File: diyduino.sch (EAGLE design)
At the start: 22 parts, among them Q2 16MHz

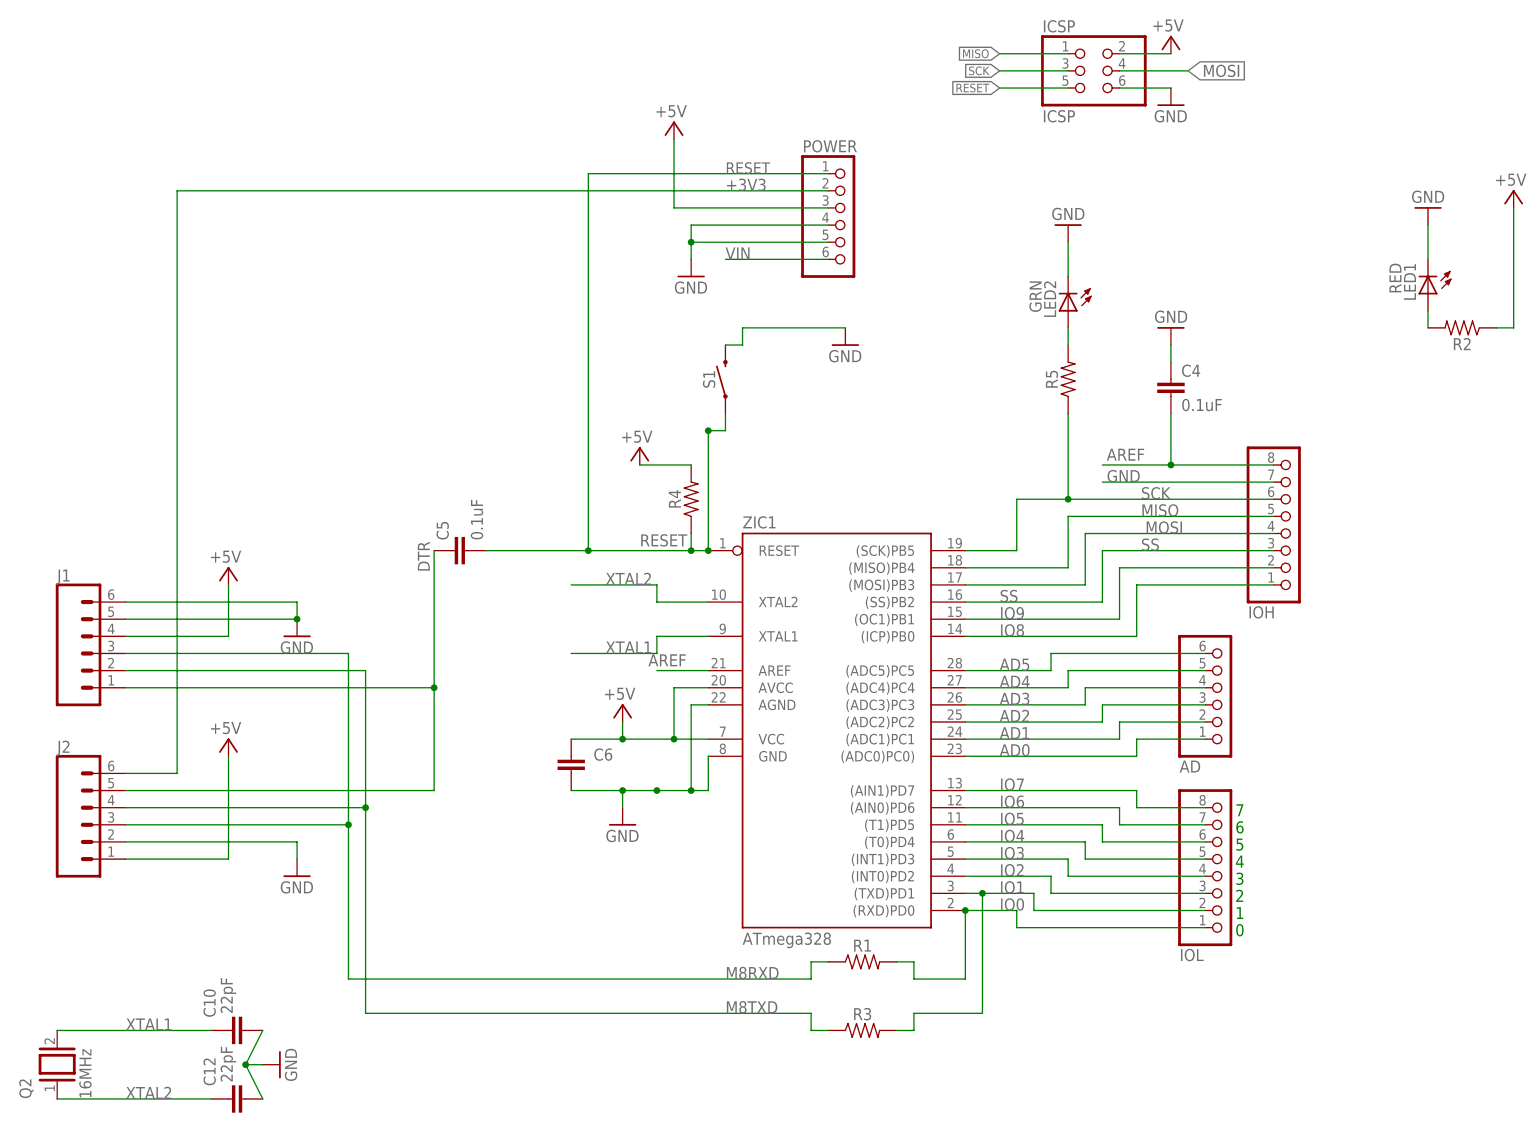
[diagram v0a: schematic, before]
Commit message: 0.3.0 changes, fixed CH340 pinout, changed crystal to resonator
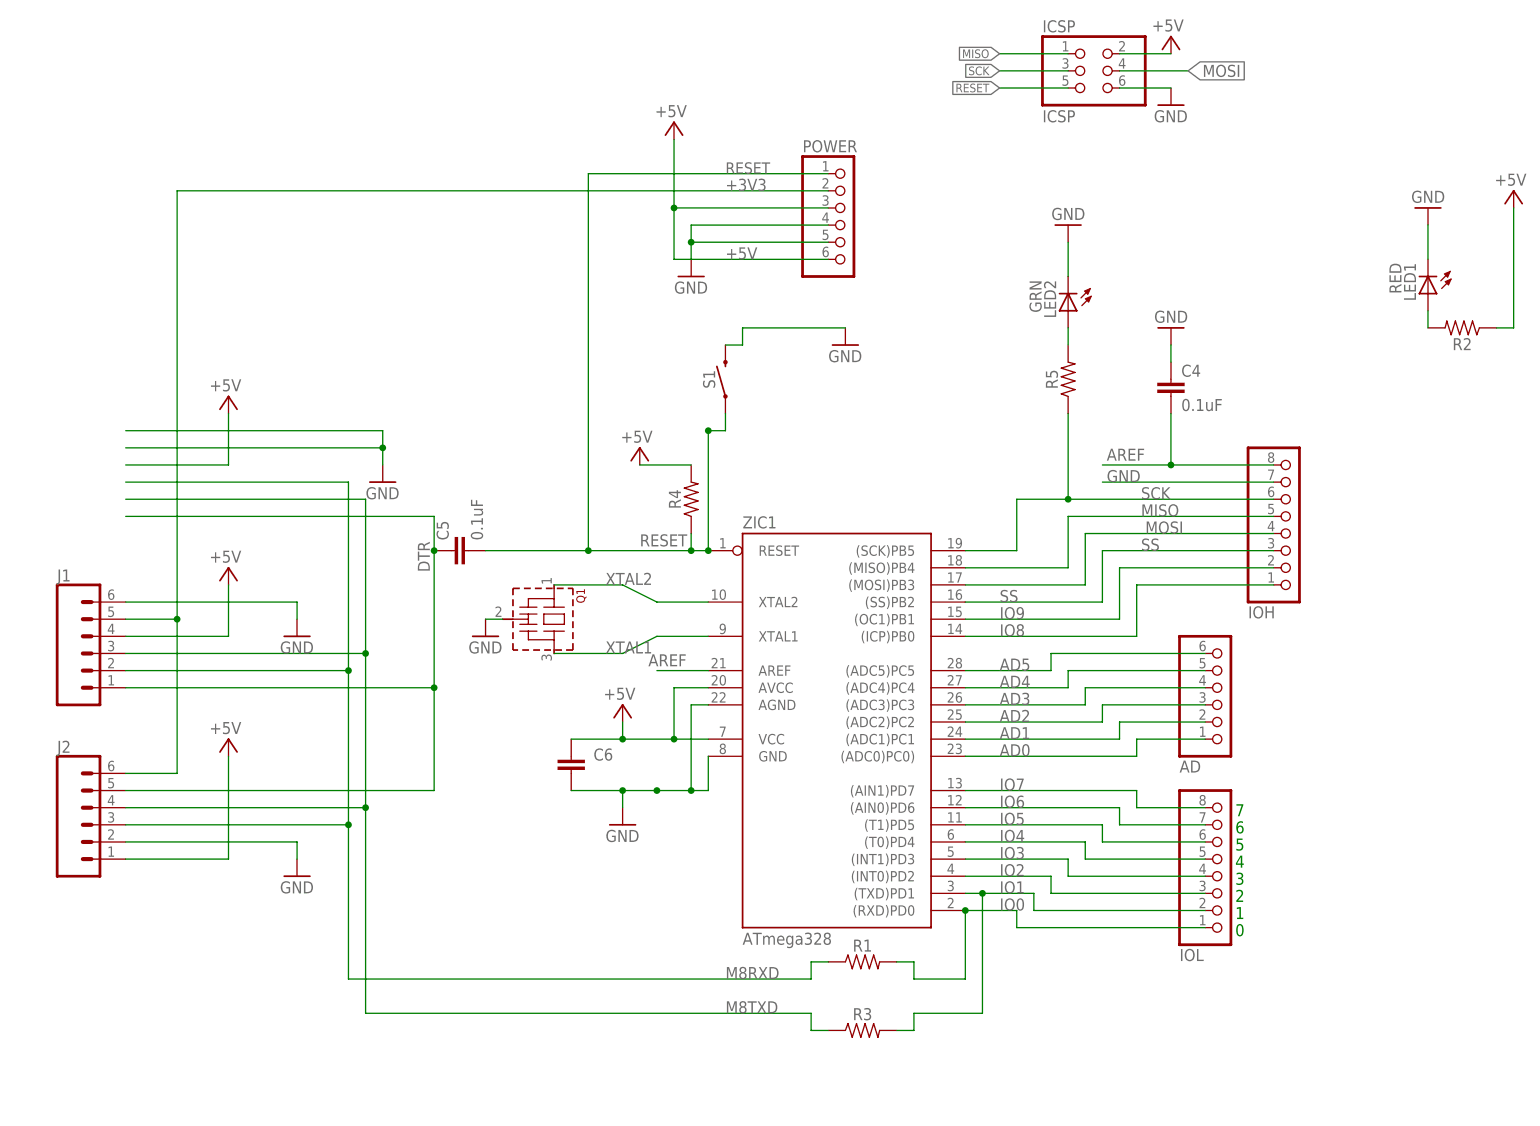
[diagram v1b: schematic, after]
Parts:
- removed C10, C12: 22pF, SparkFun-Capacitors:22PF-PTH-2.54MM-200V-5%
- removed Q2: 16MHz, special:XTAL/S
- added Q1: (no value), murata-resonators:CSTLS_X
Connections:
- removed net VIN: POWER.6
- net +3V3: now also J1.5
- net +5V: now also POWER.6
- net GND: now also Q1.VSS; no longer C10.1, C12.1, J1.5
- net M8RXD: now also J1.2; no longer J1.3
- net M8TXD: now also J1.3; no longer J1.2
- net XTAL1: now also Q1.3; no longer C10.2, Q2.2
- net XTAL2: now also Q1.1; no longer C12.2, Q2.1

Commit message: adding dinosaur!
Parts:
- renumbered C4 to C3, C5 to C1, C6 to C2
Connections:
- net +5V: now also R3.1, R5.2; no longer R2.1, R4.2
- net IO1: now also R2.2; no longer R3.2
- net M8TXD: now also R2.1; no longer R3.1
- net N$1: now also R4.2; no longer R5.2
- net N$2: now also R3.2; no longer R2.2
- net RESET: now also R5.1; no longer R4.1
- net SCK: now also R4.1; no longer R5.1
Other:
- moved on the sheet: R2, R3, R4, R5
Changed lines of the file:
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@@
 <part name="GND12" library="supply1" library_urn="urn:adsk.eagle:library:371" deviceset="GND" device=""/>
 <part name="POWER" library="pinhead" library_urn="urn:adsk.eagle:library:325" deviceset="PINHD-1X6" device="" package3d_urn="urn:adsk.eagle:package:22472/2"/>
-<part name="C4" library="capacitor-wima" library_urn="urn:adsk.eagle:library:116" deviceset="C" device="2.5/2" package3d_urn="urn:adsk.eagle:package:5415/1" value="0.1uF"/>
+<part name="C3" library="capacitor-wima" library_urn="urn:adsk.eagle:library:116" deviceset="C" device="2.5/2" package3d_urn="urn:adsk.eagle:package:5415/1" value="0.1uF"/>
 <part name="GND13" library="supply1" library_urn="urn:adsk.eagle:library:371" deviceset="GND" device=""/>
 <part name="LED2" library="adafruit" deviceset="LED" device="3MM" value="GRN"/>
 <part name="GND17" library="supply1" library_urn="urn:adsk.eagle:library:371" deviceset="GND" device=""/>
-<part name="C5" library="capacitor-wima" library_urn="urn:adsk.eagle:library:116" deviceset="C" device="2.5/2" package3d_urn="urn:adsk.eagle:package:5415/1" value="0.1uF"/>
-<part name="C6" library="capacitor-wima" library_urn="urn:adsk.eagle:library:116" deviceset="C" device="2.5/2" package3d_urn="urn:adsk.eagle:package:5415/1" value="0.1uF"/>
+<part name="C1" library="capacitor-wima" library_urn="urn:adsk.eagle:library:116" deviceset="C" device="2.5/2" package3d_urn="urn:adsk.eagle:package:5415/1" value="0.1uF"/>
+<part name="C2" library="capacitor-wima" library_urn="urn:adsk.eagle:library:116" deviceset="C" device="2.5/2" package3d_urn="urn:adsk.eagle:package:5415/1" value="0.1uF"/>
 <part name="R1" library="SparkFun-Resistors" library_urn="urn:adsk.eagle:library:532" deviceset="RESISTOR" device="AXIAL-0.3" package3d_urn="urn:adsk.eagle:package:39658/1" value=" "/>
-<part name="R3" library="SparkFun-Resistors" library_urn="urn:adsk.eagle:library:532" deviceset="RESISTOR" device="AXIAL-0.3" package3d_urn="urn:adsk.eagle:package:39658/1" value=" "/>
+<part name="R2" library="SparkFun-Resistors" library_urn="urn:adsk.eagle:library:532" deviceset="RESISTOR" device="AXIAL-0.3" package3d_urn="urn:adsk.eagle:package:39658/1" value=" "/>
+<part name="R5" library="SparkFun-Resistors" library_urn="urn:adsk.eagle:library:532" deviceset="RESISTOR" device="AXIAL-0.3" package3d_urn="urn:adsk.eagle:package:39658/1" value=" "/>
 <part name="R4" library="SparkFun-Resistors" library_urn="urn:adsk.eagle:library:532" deviceset="RESISTOR" device="AXIAL-0.3" package3d_urn="urn:adsk.eagle:package:39658/1" value=" "/>
-<part name="R5" library="SparkFun-Resistors" library_urn="urn:adsk.eagle:library:532" deviceset="RESISTOR" device="AXIAL-0.3" package3d_urn="urn:adsk.eagle:package:39658/1" value=" "/>
 <part name="J1" library="SparkFun-Connectors" library_urn="urn:adsk.eagle:library:513" deviceset="CONN_06" device="SILK_FEMALE_PTH" package3d_urn="urn:adsk.eagle:package:38009/1"/>
 <part name="GND4" library="supply1" library_urn="urn:adsk.eagle:library:371" deviceset="GND" device=""/>
@@
 <part name="LED1" library="adafruit" deviceset="LED" device="3MM" value="RED"/>
 <part name="GND6" library="supply1" library_urn="urn:adsk.eagle:library:371" deviceset="GND" device=""/>
-<part name="R2" library="SparkFun-Resistors" library_urn="urn:adsk.eagle:library:532" deviceset="RESISTOR" device="AXIAL-0.3" package3d_urn="urn:adsk.eagle:package:39658/1" value=" "/>
+<part name="R3" library="SparkFun-Resistors" library_urn="urn:adsk.eagle:library:532" deviceset="RESISTOR" device="AXIAL-0.3" package3d_urn="urn:adsk.eagle:package:39658/1" value=" "/>
 <part name="P+7" library="supply1" library_urn="urn:adsk.eagle:library:371" deviceset="+5V" device=""/>
 <part name="P+8" library="supply1" library_urn="urn:adsk.eagle:library:371" deviceset="+5V" device=""/>
@@
 <instance part="GND12" gate="1" x="157.48" y="109.22"/>
 <instance part="POWER" gate="A" x="157.48" y="127"/>
-<instance part="C4" gate="G$1" x="205.74" y="104.14"/>
+<instance part="C3" gate="G$1" x="205.74" y="104.14"/>
 <instance part="GND13" gate="1" x="205.74" y="111.76" rot="R180"/>
 <instance part="LED2" gate="G$1" x="190.5" y="114.3" rot="R180"/>
 <instance part="GND17" gate="1" x="190.5" y="127" rot="R180"/>
-<instance part="C5" gate="G$1" x="99.06" y="78.74" rot="R90"/>
-<instance part="C6" gate="G$1" x="116.84" y="45.72" smashed="yes" rot="MR180">
+<instance part="C1" gate="G$1" x="99.06" y="78.74" rot="R90"/>
+<instance part="C2" gate="G$1" x="116.84" y="45.72" smashed="yes" rot="MR180">
 <attribute name="NAME" x="123.063" y="47.625" size="1.778" layer="95" rot="MR0"/>
 </instance>
 <instance part="R1" gate="G$1" x="160.02" y="17.78"/>
-<instance part="R3" gate="G$1" x="160.02" y="7.62"/>
-<instance part="R4" gate="G$1" x="134.62" y="86.36" rot="R90"/>
-<instance part="R5" gate="G$1" x="190.5" y="104.14" rot="R90"/>
+<instance part="R2" gate="G$1" x="160.02" y="7.62"/>
+<instance part="R5" gate="G$1" x="134.62" y="86.36" rot="R90"/>
+<instance part="R4" gate="G$1" x="190.5" y="104.14" rot="R90"/>
 <instance part="J1" gate="G$1" x="45.72" y="63.5"/>
 <instance part="GND4" gate="1" x="76.2" y="66.04"/>
@@
 <instance part="LED1" gate="G$1" x="243.84" y="116.84" rot="R180"/>
 <instance part="GND6" gate="1" x="243.84" y="129.54" rot="R180"/>
-<instance part="R2" gate="G$1" x="248.92" y="111.76" rot="R180"/>
+<instance part="R3" gate="G$1" x="248.92" y="111.76" rot="R180"/>
 <instance part="P+7" gate="1" x="256.54" y="132.08" smashed="yes">
 <attribute name="VALUE" x="258.445" y="134.62" size="1.778" layer="96" rot="R180"/>
@@
 <wire x1="127" y1="91.44" x2="134.62" y2="91.44" width="0.1524" layer="91"/>
 <pinref part="P+2" gate="1" pin="+5V"/>
-<pinref part="R4" gate="G$1" pin="2"/>
+<pinref part="R5" gate="G$1" pin="2"/>
 </segment>
 <segment>
@@
 <pinref part="P+3" gate="1" pin="+5V"/>
 <pinref part="ZIC1" gate="G$1" pin="AVCC"/>
-<pinref part="C6" gate="G$1" pin="2"/>
+<pinref part="C2" gate="G$1" pin="2"/>
 </segment>
 <segment>
@@
 </segment>
 <segment>
-<pinref part="R2" gate="G$1" pin="1"/>
+<pinref part="R3" gate="G$1" pin="1"/>
 <pinref part="P+7" gate="1" pin="+5V"/>
 <wire x1="254" y1="111.76" x2="256.54" y2="111.76" width="0.1524" layer="91"/>
@@
 <pinref part="ZIC1" gate="G$1" pin="GND"/>
 <pinref part="ZIC1" gate="G$1" pin="AGND"/>
-<pinref part="C6" gate="G$1" pin="1"/>
+<pinref part="C2" gate="G$1" pin="1"/>
 </segment>
 <segment>
@@
 </segment>
 <segment>
-<pinref part="C4" gate="G$1" pin="1"/>
+<pinref part="C3" gate="G$1" pin="1"/>
 <pinref part="GND13" gate="1" pin="GND"/>
 <wire x1="205.74" y1="109.22" x2="205.74" y2="106.68" width="0.1524" layer="91"/>
@@
 <label x="196.215" y="92.075" size="1.778" layer="95"/>
 <pinref part="IOH" gate="A" pin="8"/>
-<pinref part="C4" gate="G$1" pin="2"/>
+<pinref part="C3" gate="G$1" pin="2"/>
 </segment>
 </net>
@@
 <pinref part="ZIC1" gate="G$1" pin="RESET"/>
 <pinref part="POWER" gate="A" pin="1"/>
-<pinref part="C5" gate="G$1" pin="2"/>
-<pinref part="R4" gate="G$1" pin="1"/>
+<pinref part="C1" gate="G$1" pin="2"/>
+<pinref part="R5" gate="G$1" pin="1"/>
 <pinref part="S1" gate="G$1" pin="1"/>
 </segment>
@@
 <wire x1="152.4" y1="7.62" x2="152.4" y2="10.16" width="0.1524" layer="91"/>
 <label x="139.7" y="10.16" size="1.778" layer="95"/>
-<pinref part="R3" gate="G$1" pin="1"/>
+<pinref part="R2" gate="G$1" pin="1"/>
 <pinref part="J2" gate="G$1" pin="4"/>
 <wire x1="50.8" y1="40.64" x2="86.36" y2="40.64" width="0.1524" layer="91"/>
@@
 <pinref part="IOH" gate="A" pin="6"/>
 <pinref part="ZIC1" gate="G$1" pin="(SCK)PB5"/>
-<pinref part="R5" gate="G$1" pin="1"/>
+<pinref part="R4" gate="G$1" pin="1"/>
 </segment>
 <segment>
@@
 <wire x1="50.8" y1="58.42" x2="96.52" y2="58.42" width="0.1524" layer="91"/>
 <label x="95.885" y="75.565" size="1.778" layer="95" rot="R90"/>
-<pinref part="C5" gate="G$1" pin="1"/>
+<pinref part="C1" gate="G$1" pin="1"/>
 <pinref part="J1" gate="G$1" pin="1"/>
 <pinref part="J2" gate="G$1" pin="5"/>
@@
 <pinref part="IOL" gate="A" pin="2"/>
 <pinref part="ZIC1" gate="G$1" pin="(TXD)PD1"/>
-<pinref part="R3" gate="G$1" pin="2"/>
+<pinref part="R2" gate="G$1" pin="2"/>
 </segment>
 </net>
@@
 <pinref part="LED2" gate="G$1" pin="A"/>
 <wire x1="190.5" y1="109.22" x2="190.5" y2="111.76" width="0.1524" layer="91"/>
-<pinref part="R5" gate="G$1" pin="2"/>
+<pinref part="R4" gate="G$1" pin="2"/>
 </segment>
 </net>
@@
 <segment>
 <pinref part="LED1" gate="G$1" pin="A"/>
-<pinref part="R2" gate="G$1" pin="2"/>
+<pinref part="R3" gate="G$1" pin="2"/>
 <wire x1="243.84" y1="114.3" x2="243.84" y2="111.76" width="0.1524" layer="91"/>
 </segment>
